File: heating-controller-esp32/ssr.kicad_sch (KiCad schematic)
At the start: 5 parts, among them U4 MOC3061M

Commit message: Initial design of schematic complete. Started laying out PCB
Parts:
- added D14: RED, LED_SMD:LED_0603_1608Metric, symbol Device:LED
- added R44: 1K, Resistor_SMD:R_0603_1608Metric, symbol Device:R
- U4: footprint (none) -> Package_DIP:DIP-6_W7.62mm; LCSC (none) -> C8918
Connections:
- net GND: now also D14.1 (K)
- net Trigger: now also R44.1
- new net: D14.2 (A), R44.2
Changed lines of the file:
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@@
   (junction (at 116.84 50.8) (diameter 0) (color 0 0 0 0)
   )
+  (junction (at 43.18 53.34) (diameter 0) (color 0 0 0 0)
+  )
   (junction (at 116.84 68.58) (diameter 0) (color 0 0 0 0)
   )
@@
     (stroke (width 0) (type default) (color 0 0 0 0))
   )
+  (wire (pts (xy 43.18 53.34) (xy 43.18 54.61))
+    (stroke (width 0) (type default) (color 0 0 0 0))
+  )
   (wire (pts (xy 105.41 53.34) (xy 105.41 50.8))
     (stroke (width 0) (type default) (color 0 0 0 0))
@@
     (stroke (width 0) (type default) (color 0 0 0 0))
   )
+  (wire (pts (xy 43.18 53.34) (xy 57.15 53.34))
+    (stroke (width 0) (type default) (color 0 0 0 0))
+  )
   (wire (pts (xy 116.84 68.58) (xy 93.98 68.58))
     (stroke (width 0) (type default) (color 0 0 0 0))
@@
     (stroke (width 0) (type default) (color 0 0 0 0))
   )
+  (wire (pts (xy 43.18 72.39) (xy 43.18 73.66))
+    (stroke (width 0) (type default) (color 0 0 0 0))
+  )
+  (wire (pts (xy 38.1 53.34) (xy 43.18 53.34))
+    (stroke (width 0) (type default) (color 0 0 0 0))
+  )
   (wire (pts (xy 85.09 58.42) (xy 93.98 58.42))
     (stroke (width 0) (type default) (color 0 0 0 0))
@@
     (stroke (width 0) (type default) (color 0 0 0 0))
   )
-  (hierarchical_label "Trigger" (shape input) (at 57.15 53.34 180)
+  (wire (pts (xy 43.18 62.23) (xy 43.18 64.77))
+    (stroke (width 0) (type default) (color 0 0 0 0))
+  )
+  (hierarchical_label "Trigger" (shape input) (at 38.1 53.34 180)
     (effects (font (size 1.27 1.27)) (justify right))
   )
@@
     (effects (font (size 1.27 1.27)) (justify left))
   )
+  (symbol (lib_id "Device:LED") (at 43.18 68.58 90) (unit 1)
+    (in_bom yes) (on_board yes)
+    (property "Reference" "D14" (id 0) (at 52.832 68.961 90)
+      (effects (font (size 1.778 1.778)) (justify left bottom))
+    )
+    (property "Value" "RED" (id 1) (at 51.308 68.072 90)
+      (effects (font (size 1.778 1.778)) (justify left top))
+    )
+    (property "Footprint" "LED_SMD:LED_0603_1608Metric" (id 2) (at 43.18 68.58 0)
+      (effects (font (size 1.27 1.27)) hide)
+    )
+    (property "Datasheet" "" (id 3) (at 43.18 68.58 0)
+      (effects (font (size 1.27 1.27)) hide)
+    )
+    (property "LCSC" "C2286" (id 4) (at 43.18 68.58 90)
+      (effects (font (size 1.27 1.27)) hide)
+    )
+    (pin "1")
+    (pin "2")
+  )
   (symbol (lib_id "Device:R") (at 93.98 62.23 180) (unit 1)
     (in_bom yes) (on_board yes) (fields_autoplaced)
@@
     (property "Reference" "U4" (id 0) (at 77.47 48.3702 0))
     (property "Value" "MOC3061M" (id 1) (at 77.47 50.9071 0))
-    (property "Footprint" "" (id 2) (at 72.39 60.96 0)
+    (property "Footprint" "Package_DIP:DIP-6_W7.62mm" (id 2) (at 72.39 60.96 0)
       (effects (font (size 1.27 1.27) italic) (justify left) hide)
     )
     (property "Datasheet" "https://www.onsemi.com/pub/Collateral/MOC3163M-D.pdf" (id 3) (at 77.47 55.88 0)
       (effects (font (size 1.27 1.27)) (justify left) hide)
+    )
+    (property "LCSC" "C8918" (id 4) (at 77.47 55.88 0)
+      (effects (font (size 1.27 1.27)) hide)
     )
     (pin "1")
@@
     (pin "2")
   )
+  (symbol (lib_id "Device:R") (at 43.18 58.42 0) (unit 1)
+    (in_bom yes) (on_board yes) (fields_autoplaced)
+    (property "Reference" "R44" (id 0) (at 44.958 57.5853 0)
+      (effects (font (size 1.27 1.27)) (justify left))
+    )
+    (property "Value" "1K" (id 1) (at 44.958 60.1222 0)
+      (effects (font (size 1.27 1.27)) (justify left))
+    )
+    (property "Footprint" "Resistor_SMD:R_0603_1608Metric" (id 2) (at 41.402 58.42 90)
+      (effects (font (size 1.27 1.27)) hide)
+    )
+    (property "Datasheet" "~" (id 3) (at 43.18 58.42 0)
+      (effects (font (size 1.27 1.27)) hide)
+    )
+    (property "LCSC" "C21190" (id 4) (at 43.18 58.42 0)
+      (effects (font (size 1.27 1.27)) hide)
+    )
+    (pin "1")
+    (pin "2")
+  )
   (symbol (lib_id "Andrew_Custom:ACS2") (at 116.84 55.88 0) (unit 1)
     (in_bom yes) (on_board yes) (fields_autoplaced)
@@
     (pin "2")
   )
+  (symbol (lib_id "power:GND") (at 43.18 73.66 0) (unit 1)
+    (in_bom yes) (on_board yes) (fields_autoplaced)
+    (property "Reference" "#PWR0178" (id 0) (at 43.18 80.01 0)
+      (effects (font (size 1.27 1.27)) hide)
+    )
+    (property "Value" "GND" (id 1) (at 43.18 78.1034 0))
+    (property "Footprint" "" (id 2) (at 43.18 73.66 0)
+      (effects (font (size 1.27 1.27)) hide)
+    )
+    (property "Datasheet" "" (id 3) (at 43.18 73.66 0)
+      (effects (font (size 1.27 1.27)) hide)
+    )
+    (pin "1")
+  )
 )

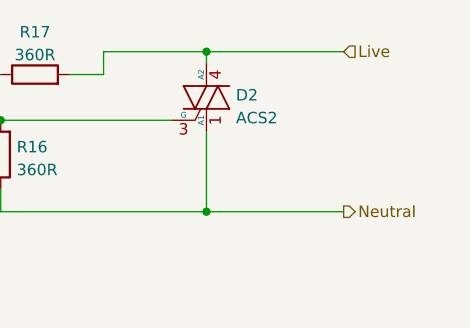
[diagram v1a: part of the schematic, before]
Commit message: Changed to Wago connectors; initial routing completed
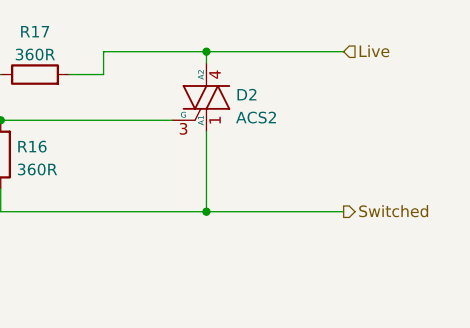
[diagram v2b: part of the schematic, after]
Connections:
- net Neutral renamed Switched
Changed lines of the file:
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@@
     (effects (font (size 1.27 1.27)) (justify right))
   )
-  (hierarchical_label "Neutral" (shape output) (at 132.08 68.58 0)
+  (hierarchical_label "Switched" (shape output) (at 132.08 68.58 0)
     (effects (font (size 1.27 1.27)) (justify left))
   )

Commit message: Mounting holes, a few more tweaks
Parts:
- R15: LCSC (none) -> C22966
- R16, R17: LCSC (none) -> C25194
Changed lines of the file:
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@@
+      (effects (font (size 1.27 1.27)) hide)
+    )
+    (property "LCSC" "C25194" (id 4) (at 93.98 62.23 0)
       (effects (font (size 1.27 1.27)) hide)
     )
@@
     )
     (property "Datasheet" "~" (id 3) (at 97.79 53.34 0)
+      (effects (font (size 1.27 1.27)) hide)
+    )
+    (property "LCSC" "C25194" (id 4) (at 97.79 53.34 0)
       (effects (font (size 1.27 1.27)) hide)
     )
@@
       (effects (font (size 1.27 1.27)) hide)
     )
+    (property "LCSC" "C22966" (id 4) (at 60.96 53.34 0)
+      (effects (font (size 1.27 1.27)) hide)
+    )

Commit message: Minor updates and update of README.md
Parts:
- R16: value 360R -> 330R; LCSC C25194 -> C23138
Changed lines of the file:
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@@
       (effects (font (size 1.27 1.27)) (justify right))
     )
-    (property "Value" "360R" (id 1) (at 95.758 63.9322 0)
+    (property "Value" "330R" (id 1) (at 95.758 63.9322 0)
       (effects (font (size 1.27 1.27)) (justify right))
     )
@@
       (effects (font (size 1.27 1.27)) hide)
     )
-    (property "LCSC" "C25194" (id 4) (at 93.98 62.23 0)
+    (property "LCSC" "C23138" (id 4) (at 93.98 62.23 0)
       (effects (font (size 1.27 1.27)) hide)
     )

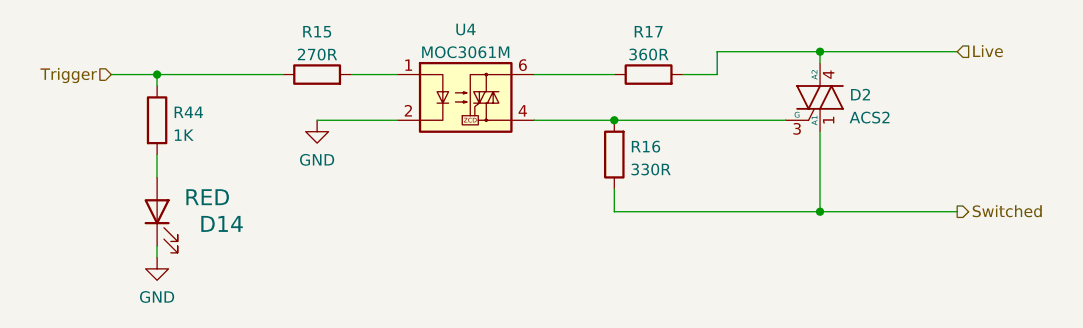
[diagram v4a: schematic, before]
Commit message: Current limiting resistors for MOC devices changed to 0.5W
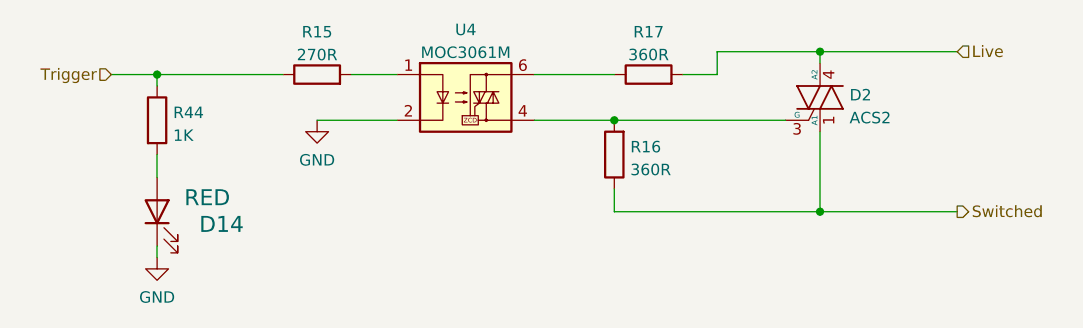
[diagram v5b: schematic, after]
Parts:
- R16: value 330R -> 360R; footprint Resistor_SMD:R_0603_1608Metric -> Resistor_SMD:R_1210_3225Metric; LCSC C23138 -> C174466
- R17: footprint Resistor_SMD:R_0603_1608Metric -> Resistor_SMD:R_1210_3225Metric; LCSC C25194 -> C174466
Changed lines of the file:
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@@
 (kicad_sch (version 20211123) (generator eeschema)
   (paper "A4")
+  (junction (at 116.84 50.8) (diameter 0) (color 0 0 0 0)
+  )
+  (junction (at 43.18 53.34) (diameter 0) (color 0 0 0 0)
+  )
   (junction (at 93.98 58.42) (diameter 0) (color 0 0 0 0)
   )
-  (junction (at 116.84 50.8) (diameter 0) (color 0 0 0 0)
-  )
-  (junction (at 43.18 53.34) (diameter 0) (color 0 0 0 0)
-  )
   (junction (at 116.84 68.58) (diameter 0) (color 0 0 0 0)
   )
@@
     (stroke (width 0) (type default) (color 0 0 0 0))
   )
+  (wire (pts (xy 93.98 58.42) (xy 113.03 58.42))
+    (stroke (width 0) (type default) (color 0 0 0 0))
+  )
   (wire (pts (xy 43.18 53.34) (xy 43.18 54.61))
     (stroke (width 0) (type default) (color 0 0 0 0))
@@
   )
   (wire (pts (xy 60.96 58.42) (xy 69.85 58.42))
-    (stroke (width 0) (type default) (color 0 0 0 0))
-  )
-  (wire (pts (xy 93.98 58.42) (xy 113.03 58.42))
     (stroke (width 0) (type default) (color 0 0 0 0))
   )
@@
     (pin "2")
   )
-  (symbol (lib_id "Device:R") (at 93.98 62.23 180) (unit 1)
-    (in_bom yes) (on_board yes) (fields_autoplaced)
-    (property "Reference" "R16" (id 0) (at 95.758 61.3953 0)
-      (effects (font (size 1.27 1.27)) (justify right))
-    )
-    (property "Value" "330R" (id 1) (at 95.758 63.9322 0)
-      (effects (font (size 1.27 1.27)) (justify right))
-    )
-    (property "Footprint" "Resistor_SMD:R_0603_1608Metric" (id 2) (at 95.758 62.23 90)
-      (effects (font (size 1.27 1.27)) hide)
-    )
-    (property "Datasheet" "~" (id 3) (at 93.98 62.23 0)
-      (effects (font (size 1.27 1.27)) hide)
-    )
-    (property "LCSC" "C23138" (id 4) (at 93.98 62.23 0)
-      (effects (font (size 1.27 1.27)) hide)
-    )
-    (pin "1")
-    (pin "2")
-  )
   (symbol (lib_id "Relay_SolidState:MOC3061M") (at 77.47 55.88 0) (unit 1)
     (in_bom yes) (on_board yes) (fields_autoplaced)
@@
     (property "Reference" "R17" (id 0) (at 97.79 48.6242 90))
     (property "Value" "360R" (id 1) (at 97.79 51.1611 90))
-    (property "Footprint" "Resistor_SMD:R_0603_1608Metric" (id 2) (at 97.79 55.118 90)
+    (property "Footprint" "Resistor_SMD:R_1210_3225Metric" (id 2) (at 97.79 55.118 90)
       (effects (font (size 1.27 1.27)) hide)
     )
@@
       (effects (font (size 1.27 1.27)) hide)
     )
-    (property "LCSC" "C25194" (id 4) (at 97.79 53.34 0)
+    (property "LCSC" "C174466" (id 4) (at 97.79 53.34 0)
       (effects (font (size 1.27 1.27)) hide)
     )
@@
     (pin "4")
   )
+  (symbol (lib_id "Device:R") (at 93.98 62.23 180) (unit 1)
+    (in_bom yes) (on_board yes) (fields_autoplaced)
+    (property "Reference" "R16" (id 0) (at 95.758 61.3953 0)
+      (effects (font (size 1.27 1.27)) (justify right))
+    )
+    (property "Value" "360R" (id 1) (at 95.758 63.9322 0)
+      (effects (font (size 1.27 1.27)) (justify right))
+    )
+    (property "Footprint" "Resistor_SMD:R_1210_3225Metric" (id 2) (at 95.758 62.23 90)
+      (effects (font (size 1.27 1.27)) hide)
+    )
+    (property "Datasheet" "~" (id 3) (at 93.98 62.23 0)
+      (effects (font (size 1.27 1.27)) hide)
+    )
+    (property "LCSC" "C174466" (id 4) (at 93.98 62.23 0)
+      (effects (font (size 1.27 1.27)) hide)
+    )
+    (pin "1")
+    (pin "2")
+  )
   (symbol (lib_id "Device:R") (at 60.96 53.34 90) (unit 1)
